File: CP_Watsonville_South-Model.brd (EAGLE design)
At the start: 150 x 100 mm, 88 parts, among them IC1 MCP23017SO, IC2 MCP23017SO, IC3 MCP23017SO

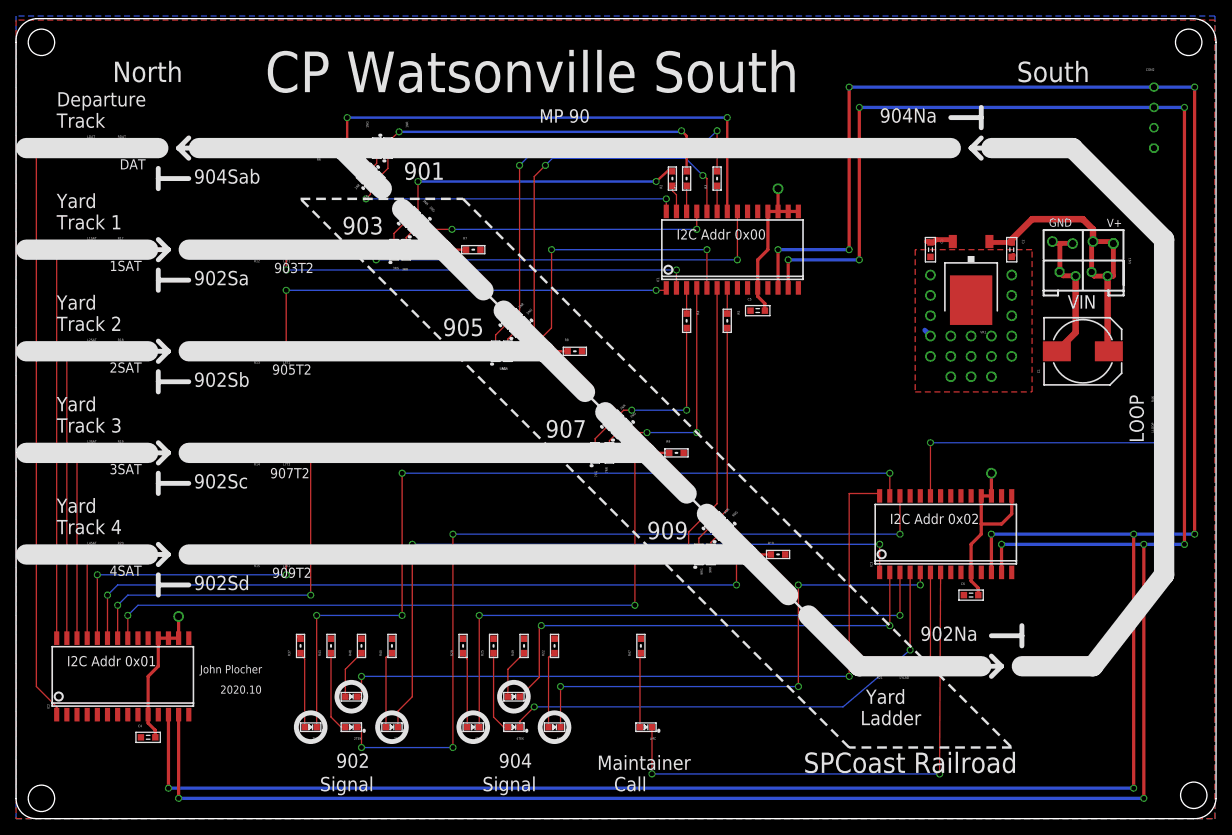
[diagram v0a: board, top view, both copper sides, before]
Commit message: Added 1x6 for MID-model board
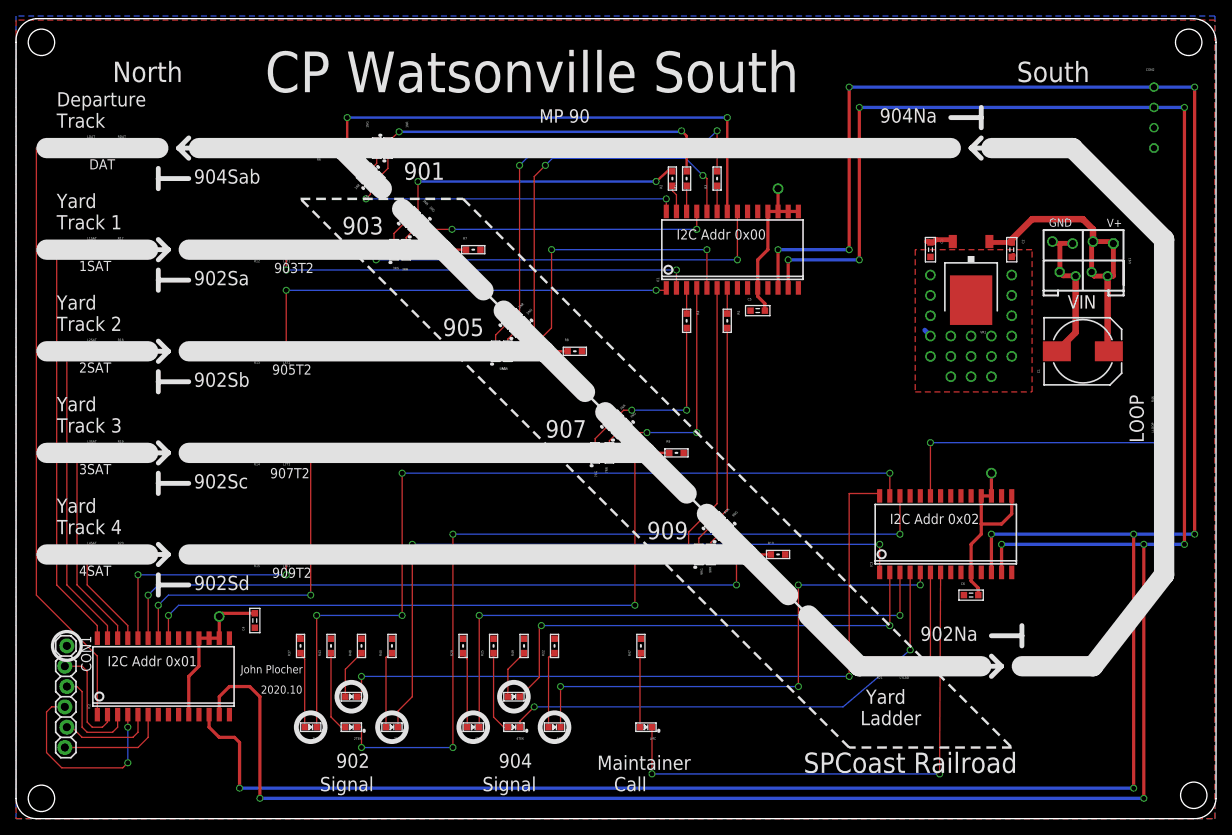
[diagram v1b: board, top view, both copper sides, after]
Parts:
- added CON1: (no value), SPCoast:1X06_LOCK
- moved C4 19.8 mm to (29.8, 24.8), turned to 90 degrees
- moved IC2 5.08 mm to (17.8, 17.8)
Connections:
- new net 1SAAT: CON1.3, IC2.3
- new net 2SAAT: CON1.4, IC2.4
- new net 3SAAT: CON1.5, IC2.5
- new net 4SAAT: CON1.6, IC2.6
- new net DAAT: CON1.2, IC2.2
- net VCC: now also CON1.1
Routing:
- net 2SAAT: track 0.00 -> 24.9 mm, vias 0 -> 2
- net 4SAAT: track 0.00 -> 13.8 mm
- net DAAT: track 0.00 -> 13.4 mm
- net 1SAAT: track 0.00 -> 13.2 mm
- net 3SAAT: track 0.00 -> 11.9 mm
- net SCL: track 324.8 -> 318.6 mm
- net 7T1: track 85.8 -> 80.7 mm
- net 9T2: track 34.1 -> 29.0 mm
- net 7T2: track 49.6 -> 44.5 mm
- net 9T1: track 88.3 -> 83.3 mm
- net DAT: track 78.7 -> 80.8 mm
- net 4SAT: track 11.0 -> 13.1 mm
- net 3SAT: track 24.9 -> 27.1 mm
- net 2SAT: track 38.9 -> 41.0 mm
- net 1SAT: track 52.9 -> 55.0 mm
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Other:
- board text added: "To MID-Model"
